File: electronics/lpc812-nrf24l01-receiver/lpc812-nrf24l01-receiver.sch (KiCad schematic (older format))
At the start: 21 parts, among them K1 BAT, K2 CH3, K3 TH, K4 ST, P1 NRF24L01+, SW1 ISP/BIND, U1 MCP1703T-3302E/CB, U2 LPC812M101JDH16_TSSOP16, X1 12 MHz

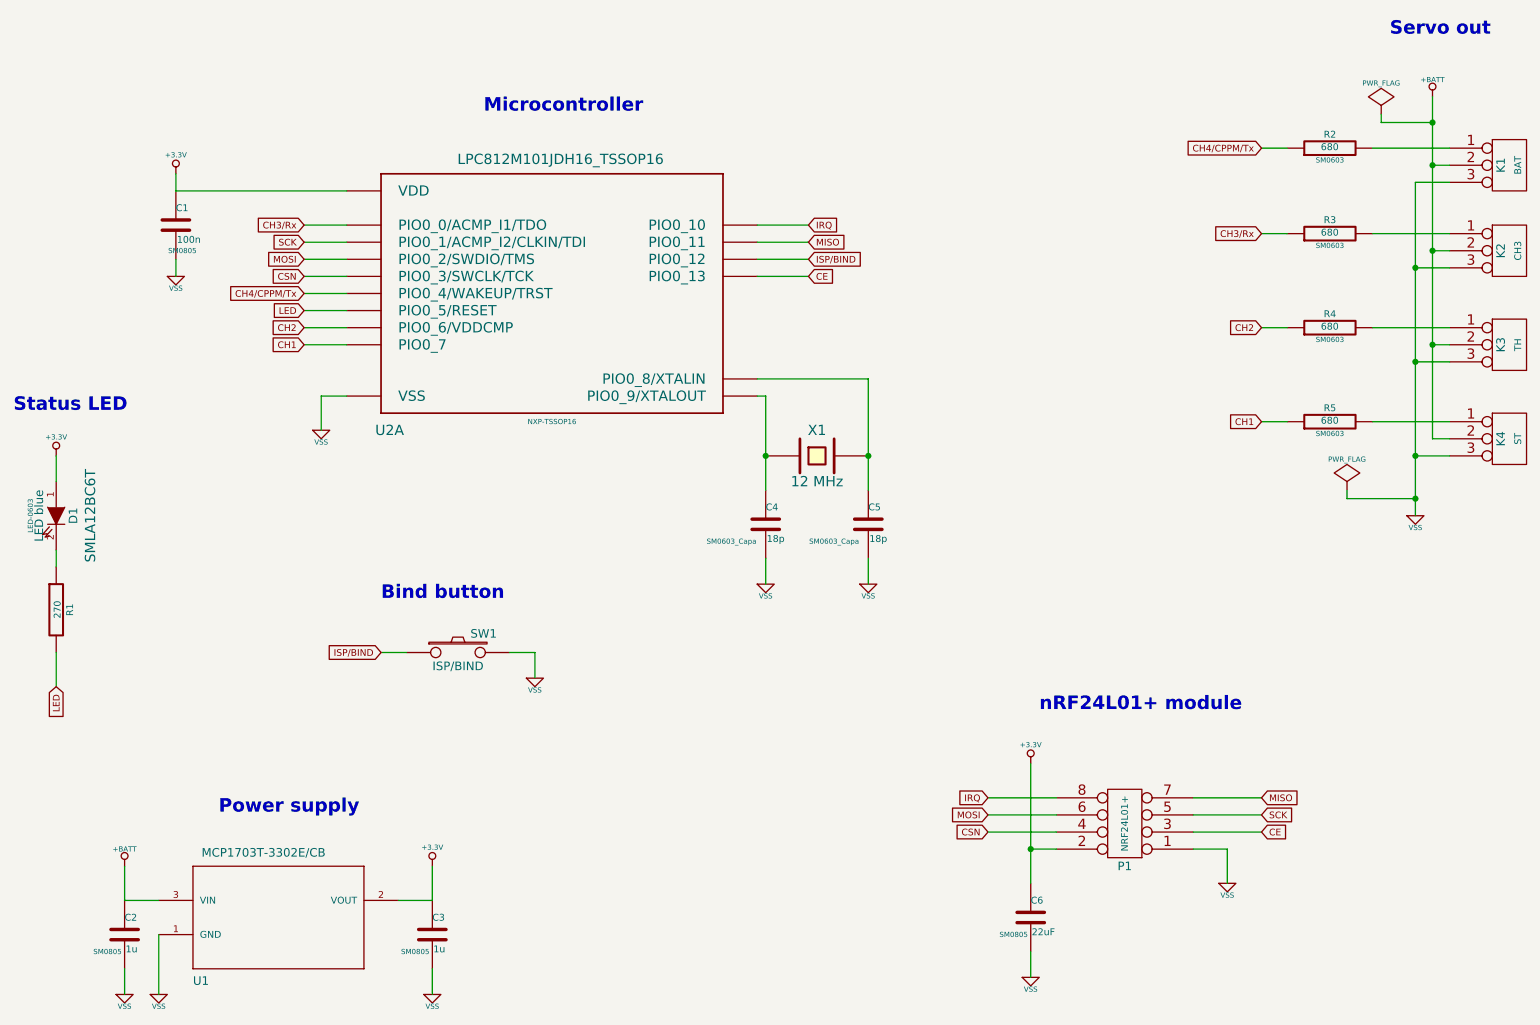
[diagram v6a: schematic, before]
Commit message: Make labels local
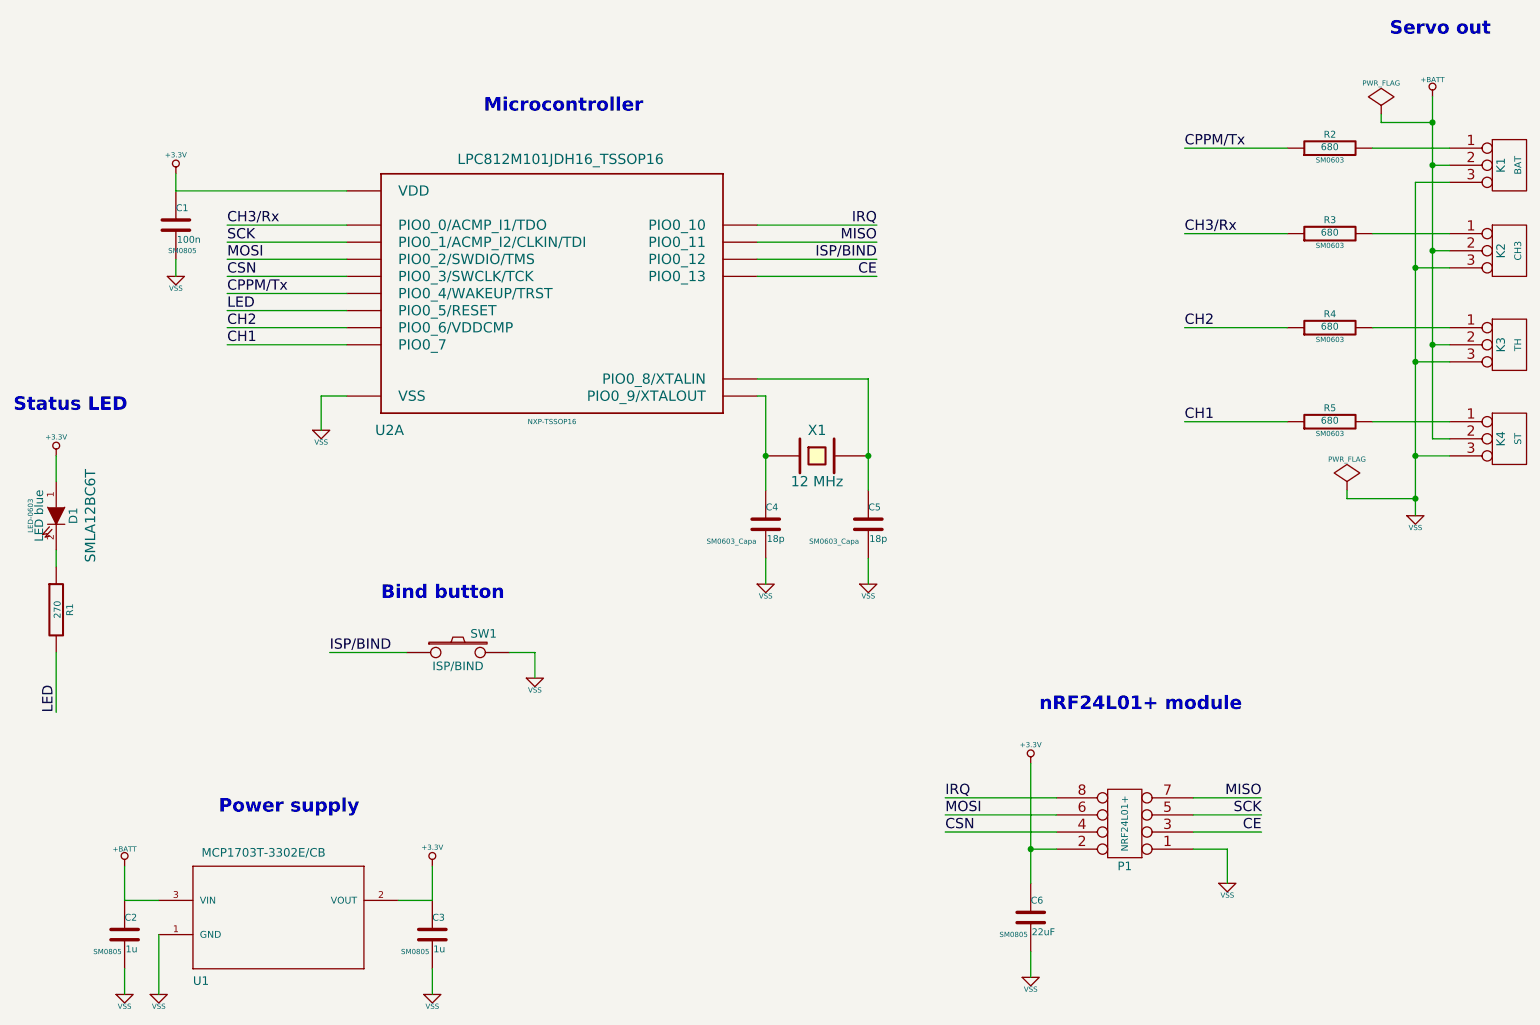
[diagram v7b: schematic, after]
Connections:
- net CH4/CPPM/Tx renamed CPPM/Tx
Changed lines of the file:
@@
 Sheet 1 1
 Title ""
-Date "23 nov 2014"
+Date "24 nov 2014"
 Rev ""
 Comp ""
@@
 	1    0    0    -1
 $EndComp
-Text GLabel 6100 2200 2    39   Input ~ 0
-MISO
-Text GLabel 8750 2150 0    39   Input ~ 0
-CH3/Rx
-Text GLabel 8750 2700 0    39   Input ~ 0
-CH2
-Text GLabel 8750 3250 0    39   Input ~ 0
-CH1
-Text GLabel 6100 2300 2    39   Input ~ 0
-ISP/BIND
-Text GLabel 6100 2400 2    39   Input ~ 0
-CE
-Text GLabel 6100 2100 2    39   Input ~ 0
-IRQ
-Text GLabel 3150 2100 0    39   Input ~ 0
-CH3/Rx
-Text GLabel 3150 2400 0    39   Input ~ 0
-CSN
-Text GLabel 3150 2200 0    39   Input ~ 0
-SCK
-Text GLabel 3150 2500 0    39   Input ~ 0
-CH4/CPPM/Tx
-Text GLabel 3150 2600 0    39   Input ~ 0
-LED
-Text GLabel 3150 2300 0    39   Input ~ 0
-MOSI
-Text GLabel 3150 2700 0    39   Input ~ 0
-CH2
-Text GLabel 7150 5550 0    39   Input ~ 0
-MOSI
-Text GLabel 8750 5450 2    39   Input ~ 0
-MISO
-Text GLabel 8750 5550 2    39   Input ~ 0
-SCK
-Text GLabel 8750 5650 2    39   Input ~ 0
-CE
-Text GLabel 7150 5450 0    39   Input ~ 0
-IRQ
-Text GLabel 7150 5650 0    39   Input ~ 0
-CSN
 $Comp
 L VSS #PWR06
@@
 	1    0    0    -1
 $EndComp
-Text GLabel 3150 2800 0    39   Input ~ 0
-CH1
-Text GLabel 8750 1650 0    39   Input ~ 0
-CH4/CPPM/Tx
 $Comp
 L SW_PUSH SW1
@@
 	1    0    0    -1
 $EndComp
-Text GLabel 3600 4600 0    39   Input ~ 0
-ISP/BIND
 $Comp
 L LED D1
@@
 	1    0    0    -1
 $EndComp
-Text GLabel 1700 4800 3    39   Input ~ 0
-LED
 $Comp
 L LPC812M101JDH16_TSSOP16 U2
@@
 	9400 1650 9850 1650
 Wire Wire Line
-	3400 2100 3150 2100
-Wire Wire Line
-	3400 2300 3150 2300
-Wire Wire Line
-	3400 2400 3150 2400
-Wire Wire Line
-	3150 2500 3400 2500
-Wire Wire Line
-	3400 2600 3150 2600
-Wire Wire Line
-	3400 2700 3150 2700
-Wire Wire Line
-	3400 2800 3150 2800
-Wire Wire Line
-	5800 2400 6100 2400
+	3400 2100 2700 2100
+Wire Wire Line
+	3400 2300 2700 2300
+Wire Wire Line
+	3400 2400 2700 2400
+Wire Wire Line
+	2700 2500 3400 2500
+Wire Wire Line
+	3400 2600 2700 2600
+Wire Wire Line
+	3400 2700 2700 2700
+Wire Wire Line
+	3400 2800 2700 2800
+Wire Wire Line
+	5800 2400 6500 2400
 Wire Wire Line
 	8350 5750 8550 5750
@@
 	8350 5450 8750 5450
 Wire Wire Line
-	7550 5450 7150 5450
-Wire Wire Line
-	7550 5550 7150 5550
-Wire Wire Line
-	7550 5650 7150 5650
-Wire Wire Line
-	5800 2100 6100 2100
-Wire Wire Line
-	5800 2200 6100 2200
+	7550 5450 6900 5450
+Wire Wire Line
+	7550 5550 6900 5550
+Wire Wire Line
+	7550 5650 6900 5650
+Wire Wire Line
+	5800 2100 6500 2100
+Wire Wire Line
+	5800 2200 6500 2200
 Wire Wire Line
 	3900 6600 3900 6450
@@
 	6450 4050 6450 4200
 Wire Wire Line
-	3400 2200 3150 2200
+	3400 2200 2700 2200
 Wire Wire Line
 	4350 4600 4500 4600
@@
 	4500 4600 4500 4750
 Wire Wire Line
-	3750 4600 3600 4600
+	3750 4600 3300 4600
 Wire Wire Line
 	1700 3450 1700 3600
@@
 	1700 4000 1700 4100
 Wire Wire Line
-	1700 4600 1700 4800
+	1700 4600 1700 4950
 Wire Wire Line
 	5850 3100 5800 3100
 Wire Wire Line
-	5800 2300 6100 2300
+	5800 2300 6500 2300
 Wire Wire Line
 	6450 3000 5800 3000
@@
 $EndComp
 Wire Wire Line
-	8750 3250 8900 3250
-Wire Wire Line
-	8750 2700 8900 2700
-Wire Wire Line
-	8750 2150 8900 2150
-Wire Wire Line
-	8750 1650 8900 1650
+	8300 3250 8900 3250
+Wire Wire Line
+	8300 2700 8900 2700
+Wire Wire Line
+	8300 2150 8900 2150
+Wire Wire Line
+	8300 1650 8900 1650
+Text Label 6500 2300 2    60   ~ 0
+ISP/BIND
+Text Label 3300 4600 0    60   ~ 0
+ISP/BIND
+Text Label 8300 1650 0    60   ~ 0
+CPPM/Tx
+Text Label 8300 2150 0    60   ~ 0
+CH3/Rx
+Text Label 8300 2700 0    60   ~ 0
+CH2
+Text Label 8300 3250 0    60   ~ 0
+CH1
+Text Label 2700 2100 0    60   ~ 0
+CH3/Rx
+Text Label 2700 2500 0    60   ~ 0
+CPPM/Tx
+Text Label 2700 2800 0    60   ~ 0
+CH1
+Text Label 2700 2700 0    60   ~ 0
+CH2
+Text Label 6500 2100 2    60   ~ 0
+IRQ
+Text Label 6500 2200 2    60   ~ 0
+MISO
+Text Label 6500 2400 2    60   ~ 0
+CE
+Text Label 6900 5450 0    60   ~ 0
+IRQ
+Text Label 6900 5550 0    60   ~ 0
+MOSI
+Text Label 6900 5650 0    60   ~ 0
+CSN
+Text Label 8750 5450 2    60   ~ 0
+MISO
+Text Label 8750 5550 2    60   ~ 0
+SCK
+Text Label 8750 5650 2    60   ~ 0
+CE
+Text Label 1700 4950 1    60   ~ 0
+LED
+Text Label 2700 2600 0    60   ~ 0
+LED
+Text Label 2700 2400 0    60   ~ 0
+CSN
+Text Label 2700 2300 0    60   ~ 0
+MOSI
+Text Label 2700 2200 0    60   ~ 0
+SCK
 $EndSCHEMATC

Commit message: Tweak label names
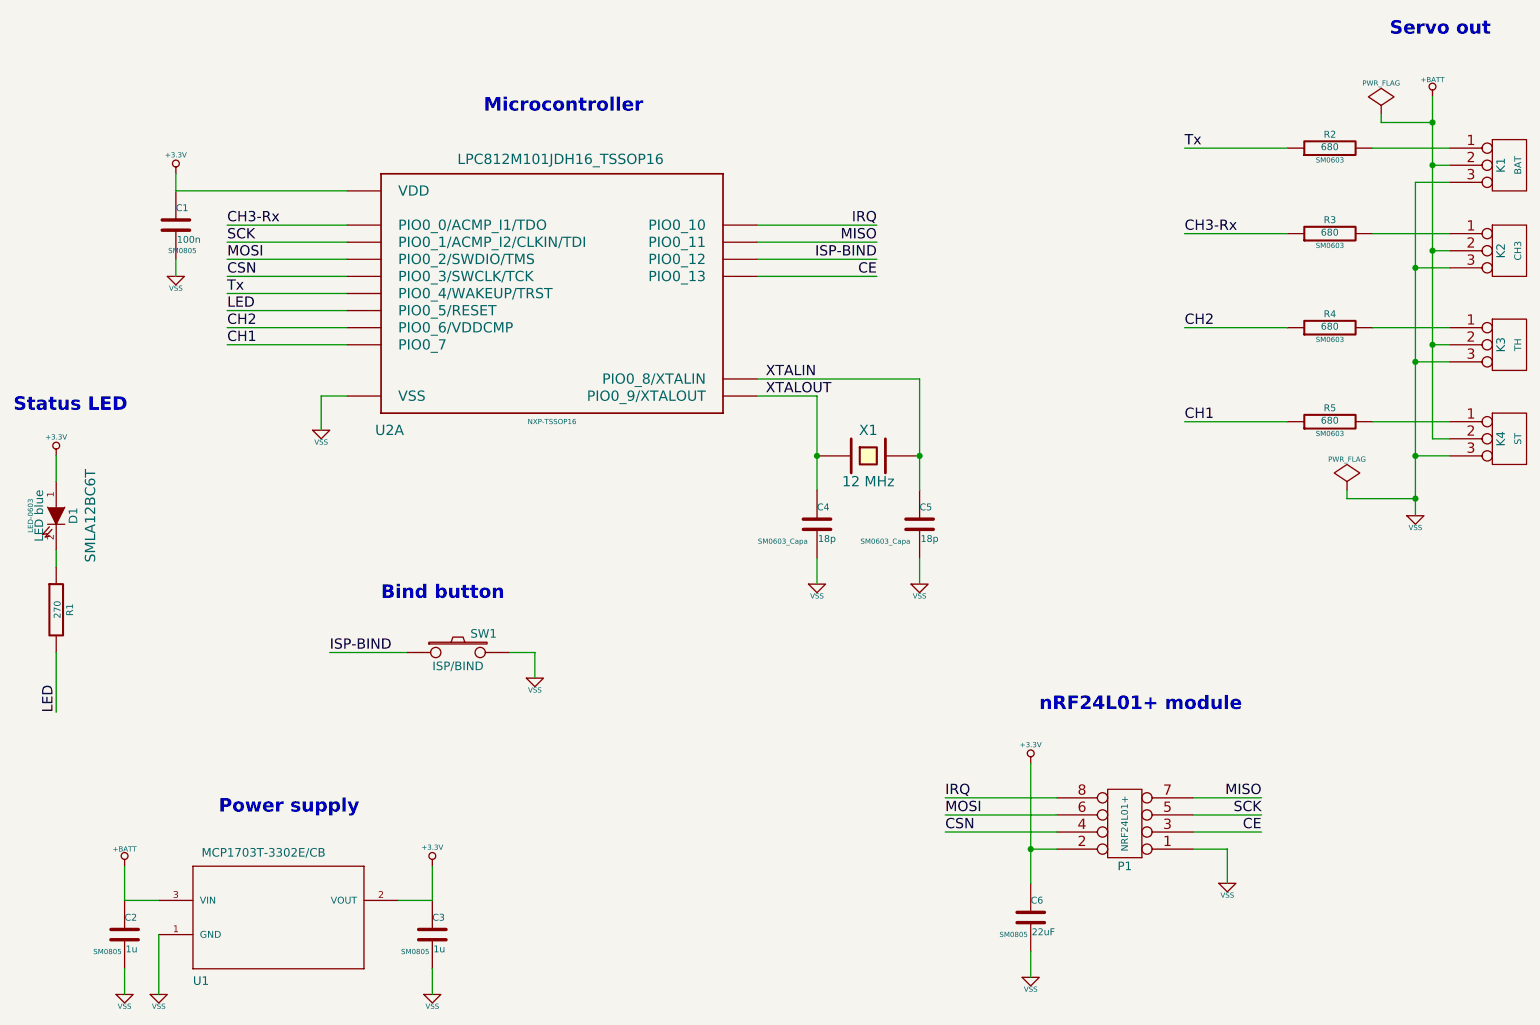
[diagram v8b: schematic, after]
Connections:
- net XTALOUT: now reaches C4.1, U2.10 (PIO0_9/XTALOUT), X1.1
- net XTALIN: now reaches C5.1, U2.11 (PIO0_8/XTALIN), X1.2
- net CH3/Rx renamed CH3-Rx
- net CPPM/Tx renamed Tx
- net ISP/BIND renamed ISP-BIND
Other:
- moved on the sheet: C4, C5, X1
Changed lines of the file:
@@
 L CRYSTAL X1
 U 1 1 546EFECA
-P 6150 3450
-F 0 "X1" H 6150 3600 60  0000 C CNN
-F 1 "12 MHz" H 6150 3300 60  0000 C CNN
-F 2 "crystal-SM49" H 6150 3450 60  0001 C CNN
-F 3 "~" H 6150 3450 60  0000 C CNN
-	1    6150 3450
+P 6450 3450
+F 0 "X1" H 6450 3600 60  0000 C CNN
+F 1 "12 MHz" H 6450 3300 60  0000 C CNN
+F 2 "crystal-SM49" H 6450 3450 60  0001 C CNN
+F 3 "~" H 6450 3450 60  0000 C CNN
+	1    6450 3450
 	1    0    0    -1
 $EndComp
@@
 L C C4
 U 1 1 546EFF7D
-P 5850 3850
-F 0 "C4" H 5850 3950 40  0000 L CNN
-F 1 "18p" H 5856 3765 40  0000 L CNN
-F 2 "SM0603_Capa" H 5650 3750 30  0000 C CNN
-F 3 "~" H 5850 3850 60  0000 C CNN
-	1    5850 3850
+P 6150 3850
+F 0 "C4" H 6150 3950 40  0000 L CNN
+F 1 "18p" H 6156 3765 40  0000 L CNN
+F 2 "SM0603_Capa" H 5950 3750 30  0000 C CNN
+F 3 "~" H 6150 3850 60  0000 C CNN
+	1    6150 3850
 	1    0    0    -1
 $EndComp
@@
 L C C5
 U 1 1 546EFF8A
-P 6450 3850
-F 0 "C5" H 6450 3950 40  0000 L CNN
-F 1 "18p" H 6456 3765 40  0000 L CNN
-F 2 "SM0603_Capa" H 6250 3750 30  0000 C CNN
-F 3 "~" H 6450 3850 60  0000 C CNN
-	1    6450 3850
+P 6750 3850
+F 0 "C5" H 6750 3950 40  0000 L CNN
+F 1 "18p" H 6756 3765 40  0000 L CNN
+F 2 "SM0603_Capa" H 6550 3750 30  0000 C CNN
+F 3 "~" H 6750 3850 60  0000 C CNN
+	1    6750 3850
 	1    0    0    -1
 $EndComp
@@
 L VSS #PWR013
 U 1 1 546F0131
-P 5850 4200
-F 0 "#PWR013" H 5850 4200 30  0001 C CNN
-F 1 "VSS" H 5850 4130 30  0000 C CNN
-F 2 "" H 5850 4200 60  0000 C CNN
-F 3 "" H 5850 4200 60  0000 C CNN
-	1    5850 4200
+P 6150 4200
+F 0 "#PWR013" H 6150 4200 30  0001 C CNN
+F 1 "VSS" H 6150 4130 30  0000 C CNN
+F 2 "" H 6150 4200 60  0000 C CNN
+F 3 "" H 6150 4200 60  0000 C CNN
+	1    6150 4200
 	1    0    0    -1
 $EndComp
@@
 L VSS #PWR014
 U 1 1 546F013E
-P 6450 4200
-F 0 "#PWR014" H 6450 4200 30  0001 C CNN
-F 1 "VSS" H 6450 4130 30  0000 C CNN
-F 2 "" H 6450 4200 60  0000 C CNN
-F 3 "" H 6450 4200 60  0000 C CNN
-	1    6450 4200
+P 6750 4200
+F 0 "#PWR014" H 6750 4200 30  0001 C CNN
+F 1 "VSS" H 6750 4130 30  0000 C CNN
+F 2 "" H 6750 4200 60  0000 C CNN
+F 3 "" H 6750 4200 60  0000 C CNN
+	1    6750 4200
 	1    0    0    -1
 $EndComp
@@
 	3900 6600 3900 6450
 Wire Wire Line
-	5850 3100 5850 3650
-Connection ~ 5850 3450
-Wire Wire Line
-	6450 3000 6450 3650
-Connection ~ 6450 3450
-Wire Wire Line
-	5850 4050 5850 4200
-Wire Wire Line
-	6450 4050 6450 4200
+	6150 3100 6150 3650
+Connection ~ 6150 3450
+Wire Wire Line
+	6750 3000 6750 3650
+Connection ~ 6750 3450
+Wire Wire Line
+	6150 4050 6150 4200
+Wire Wire Line
+	6750 4050 6750 4200
 Wire Wire Line
 	3400 2200 2700 2200
@@
 	1700 4600 1700 4950
 Wire Wire Line
-	5850 3100 5800 3100
+	6150 3100 5800 3100
 Wire Wire Line
 	5800 2300 6500 2300
 Wire Wire Line
-	6450 3000 5800 3000
+	6750 3000 5800 3000
 Wire Wire Line
 	8750 5650 8350 5650
@@
 	8300 1650 8900 1650
 Text Label 6500 2300 2    60   ~ 0
-ISP/BIND
+ISP-BIND
 Text Label 3300 4600 0    60   ~ 0
-ISP/BIND
+ISP-BIND
 Text Label 8300 1650 0    60   ~ 0
-CPPM/Tx
+Tx
 Text Label 8300 2150 0    60   ~ 0
-CH3/Rx
+CH3-Rx
 Text Label 8300 2700 0    60   ~ 0
 CH2
@@
 CH1
 Text Label 2700 2100 0    60   ~ 0
-CH3/Rx
+CH3-Rx
 Text Label 2700 2500 0    60   ~ 0
-CPPM/Tx
+Tx
 Text Label 2700 2800 0    60   ~ 0
 CH1
@@
 Text Label 6500 2400 2    60   ~ 0
 CE
-Text Label 6900 5450 0    60   ~ 0
-IRQ
 Text Label 6900 5550 0    60   ~ 0
 MOSI
@@
 Text Label 2700 2200 0    60   ~ 0
 SCK
+Text Label 6900 5450 0    60   ~ 0
+IRQ
+Text Label 5850 3000 0    60   ~ 0
+XTALIN
+Text Label 5850 3100 0    60   ~ 0
+XTALOUT
 $EndSCHEMATC
